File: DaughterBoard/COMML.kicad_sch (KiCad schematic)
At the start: 25 parts, among them J2 PEC03SAAN, J3 PEC02SAAN, J4 PEC02SAAN

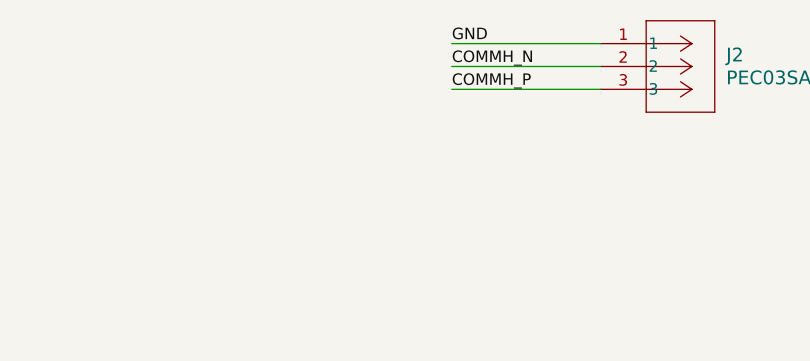
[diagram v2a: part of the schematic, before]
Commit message: DOBO ERC 139 warnings left
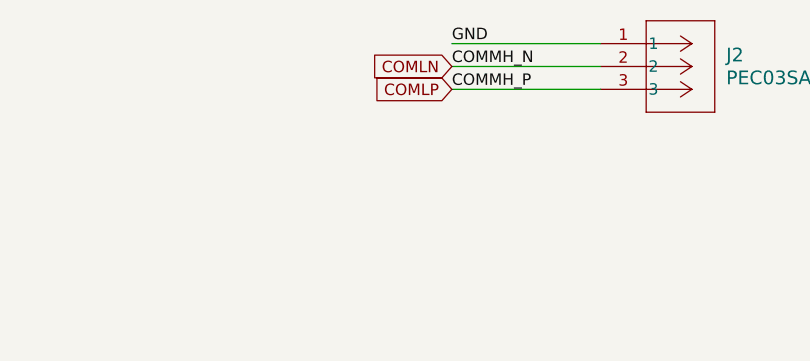
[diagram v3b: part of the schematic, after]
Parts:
- C40, C41: footprint CL10B221JB8NNNC:CAP_CL10_SAM-L -> CAP_CL10_SAM
- C42: footprint GCM1885C1H101JA16J (1):CAPC1608X90N -> GCM1885C1H101JA16J:CAPC1608X90N
- C43, C44: footprint 1206J2K00222KXR (1):CAPC3216X160N -> 1206J2K00222KXR:CAPC3216X160N
- D2: footprint PESD1CAN,215:SOT23_PESD1_NEX-L -> SOT23_PESD1_NEX
- FL1: footprint 744242471:744242471 -> 744242471
- J2: footprint PEC03SAAN:CONN_PEC03SAAN_SUL -> CONN_PEC03SAAN_SUL
- J3, J4: footprint PEC02SAAN:CONN_PxC02S_SUL -> CONN_PxC02S_SUL
- R34, R35: footprint CRCW060351R0JNEA:RC0603N_VIS-L -> RC0603N_VIS
- R36: footprint ERJ-3EKF1001V:RC0603N_PAN-L -> RC0603N_PAN
- R37, R38: footprint RC0603JR-070RL:RC0603N_YAG-L -> RC0603N_YAG
- R39, R40, R41, R42, R43, R44, R45, R46, R47, R48: footprint CRCW08050000Z0EAHP:RES_CRCW_0805_VIS-L -> RES_CRCW_0805_VIS
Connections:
- net COMMH_N is gone; now on net COMLN: J2.2
- net COMMH_P is gone; now on net COMLP: J2.3
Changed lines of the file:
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@@
+		)
+	)
+	(global_label "COMLP"
+		(shape input)
+		(at 232.41 31.75 180)
+		(fields_autoplaced yes)
+		(effects
+			(font
+				(size 1.27 1.27)
+			)
+			(justify right)
+		)
+		(property "Intersheetrefs" "${INTERSHEET_REFS}"
+			(at 223.0748 31.75 0)
+			(effects
+				(font
+					(size 1.27 1.27)
+				)
+				(justify right)
+				(hide yes)
+			)
 		)
 	)
@@
 		)
 	)
-	(symbol
+	(global_label "COMLN"
+		(shape input)
+		(at 232.41 29.21 180)
+		(fields_autoplaced yes)
+		(effects
+			(font
+				(size 1.27 1.27)
+			)
+			(justify right)
+		)
+		(property "Intersheetrefs" "${INTERSHEET_REFS}"
+			(at 223.0143 29.21 0)
+			(effects
+				(font
+					(size 1.27 1.27)
+				)
+				(justify right)
+				(hide yes)
+			)
+		)
+	)
+	(symbol
+		(lib_name "CRCW060351R0JNEA_1")
 		(lib_id "CRCW060351R0JNEA:CRCW060351R0JNEA")
 		(at 137.16 101.6 0)
@@
 			)
 		)
-		(property "Footprint" "CRCW060351R0JNEA:RC0603N_VIS-L"
+		(property "Footprint" "RC0603N_VIS"
 			(at 136.906 96.266 0)
 			(effects
@@
 			)
 		)
-		(property "Footprint" "1206J2K00222KXR (1):CAPC3216X160N"
+		(property "Footprint" "1206J2K00222KXR:CAPC3216X160N"
 			(at 102.87 176.53 0)
 			(effects
@@
 			)
 		)
-		(property "Footprint" "PEC03SAAN:CONN_PEC03SAAN_SUL"
+		(property "Footprint" "CONN_PEC03SAAN_SUL"
+			(at 249.174 36.83 0)
+			(effects
+				(font
+					(size 1.27 1.27)
+					(italic yes)
+				)
+				(hide yes)
+			)
+		)
+		(property "Datasheet" "PEC03SAAN"
+			(at 248.666 22.098 0)
+			(effects
+				(font
+					(size 1.27 1.27)
+					(italic yes)
+				)
+				(hide yes)
+			)
+		)
+		(property "Description" ""
 			(at 248.92 26.67 0)
 			(effects
 				(font
 					(size 1.27 1.27)
-					(italic yes)
-				)
-				(hide yes)
-			)
-		)
-		(property "Datasheet" "PEC03SAAN"
-			(at 248.92 26.67 0)
-			(effects
-				(font
-					(size 1.27 1.27)
-					(italic yes)
-				)
-				(hide yes)
-			)
-		)
-		(property "Description" ""
-			(at 248.92 26.67 0)
-			(effects
-				(font
-					(size 1.27 1.27)
 				)
 				(hide yes)
@@
 	)
 	(symbol
-		(lib_name "CRCW08050000Z0EAHP_2")
+		(lib_name "CRCW08050000Z0EAHP_1")
 		(lib_id "CRCW08050000Z0EAHP:CRCW08050000Z0EAHP")
 		(at 77.47 184.15 0)
@@
 			)
 		)
-		(property "Footprint" "CRCW08050000Z0EAHP:RES_CRCW_0805_VIS-L"
+		(property "Footprint" "RES_CRCW_0805_VIS"
 			(at 77.216 188.976 0)
 			(effects
@@
 	)
 	(symbol
+		(lib_name "CRCW08050000Z0EAHP_1")
 		(lib_id "CRCW08050000Z0EAHP:CRCW08050000Z0EAHP")
 		(at 68.58 31.75 0)
@@
 			)
 		)
-		(property "Footprint" "CRCW08050000Z0EAHP:RES_CRCW_0805_VIS-L"
+		(property "Footprint" "RES_CRCW_0805_VIS"
+			(at 68.072 34.798 0)
+			(effects
+				(font
+					(size 1.27 1.27)
+					(italic yes)
+				)
+				(hide yes)
+			)
+		)
+		(property "Datasheet" "CRCW08050000Z0EAHP"
+			(at 68.58 33.274 0)
+			(effects
+				(font
+					(size 1.27 1.27)
+					(italic yes)
+				)
+				(hide yes)
+			)
+		)
+		(property "Description" ""
 			(at 68.58 31.75 0)
 			(effects
 				(font
 					(size 1.27 1.27)
-					(italic yes)
-				)
-				(hide yes)
-			)
-		)
-		(property "Datasheet" "CRCW08050000Z0EAHP"
-			(at 68.58 31.75 0)
-			(effects
-				(font
-					(size 1.27 1.27)
-					(italic yes)
-				)
-				(hide yes)
-			)
-		)
-		(property "Description" ""
-			(at 68.58 31.75 0)
-			(effects
-				(font
-					(size 1.27 1.27)
 				)
 				(hide yes)
@@
 	)
 	(symbol
-		(lib_name "CRCW08050000Z0EAHP_4")
+		(lib_name "CRCW08050000Z0EAHP_1")
 		(lib_id "CRCW08050000Z0EAHP:CRCW08050000Z0EAHP")
 		(at 115.57 157.48 0)
@@
 			)
 		)
-		(property "Footprint" "CRCW08050000Z0EAHP:RES_CRCW_0805_VIS-L"
+		(property "Footprint" "RES_CRCW_0805_VIS"
 			(at 114.3 163.576 0)
 			(effects
@@
 	)
 	(symbol
+		(lib_name "PEC02SAAN_1")
 		(lib_id "PEC02SAAN:PEC02SAAN")
 		(at 242.57 154.94 0)
@@
 			)
 		)
-		(property "Footprint" "PEC02SAAN:CONN_PxC02S_SUL"
+		(property "Footprint" "CONN_PxC02S_SUL"
+			(at 242.57 162.306 0)
+			(effects
+				(font
+					(size 1.27 1.27)
+					(italic yes)
+				)
+				(hide yes)
+			)
+		)
+		(property "Datasheet" "PEC02SAAN"
+			(at 243.078 152.654 0)
+			(effects
+				(font
+					(size 1.27 1.27)
+					(italic yes)
+				)
+				(hide yes)
+			)
+		)
+		(property "Description" ""
 			(at 242.57 154.94 0)
 			(effects
 				(font
 					(size 1.27 1.27)
-					(italic yes)
-				)
-				(hide yes)
-			)
-		)
-		(property "Datasheet" "PEC02SAAN"
-			(at 242.57 154.94 0)
-			(effects
-				(font
-					(size 1.27 1.27)
-					(italic yes)
-				)
-				(hide yes)
-			)
-		)
-		(property "Description" ""
-			(at 242.57 154.94 0)
-			(effects
-				(font
-					(size 1.27 1.27)
 				)
 				(hide yes)
@@
 	)
 	(symbol
-		(lib_name "CRCW08050000Z0EAHP_5")
 		(lib_id "CRCW08050000Z0EAHP:CRCW08050000Z0EAHP")
 		(at 43.18 161.29 0)
@@
 			)
 		)
-		(property "Footprint" "CRCW08050000Z0EAHP:RES_CRCW_0805_VIS-L"
+		(property "Footprint" "RES_CRCW_0805_VIS"
 			(at 43.18 168.656 0)
 			(effects
@@
 	)
 	(symbol
-		(lib_name "CRCW08050000Z0EAHP_7")
+		(lib_name "CRCW08050000Z0EAHP_1")
 		(lib_id "CRCW08050000Z0EAHP:CRCW08050000Z0EAHP")
 		(at 115.57 176.53 0)
@@
 			)
 		)
-		(property "Footprint" "CRCW08050000Z0EAHP:RES_CRCW_0805_VIS-L"
+		(property "Footprint" "RES_CRCW_0805_VIS"
 			(at 114.808 169.926 0)
 			(effects
@@
 			)
 		)
-		(property "Footprint" "PESD1CAN,215:SOT23_PESD1_NEX-L"
+		(property "Footprint" "SOT23_PESD1_NEX"
 			(at 143.764 106.68 0)
 			(effects
@@
 			)
 		)
-		(property "Footprint" "744242471:744242471"
+		(property "Footprint" "744242471"
 			(at 92.71 260.02 0)
 			(effects
@@
 	)
 	(symbol
-		(lib_name "CRCW08050000Z0EAHP_8")
+		(lib_name "CRCW08050000Z0EAHP_1")
 		(lib_id "CRCW08050000Z0EAHP:CRCW08050000Z0EAHP")
 		(at 43.18 49.53 0)
@@
 			)
 		)
-		(property "Footprint" "CRCW08050000Z0EAHP:RES_CRCW_0805_VIS-L"
+		(property "Footprint" "RES_CRCW_0805_VIS"
 			(at 39.624 40.894 0)
 			(effects
@@
 	)
 	(symbol
-		(lib_name "CRCW08050000Z0EAHP_9")
+		(lib_name "CRCW08050000Z0EAHP_1")
 		(lib_id "CRCW08050000Z0EAHP:CRCW08050000Z0EAHP")
 		(at 43.18 31.75 0)
@@
 			)
 		)
-		(property "Footprint" "CRCW08050000Z0EAHP:RES_CRCW_0805_VIS-L"
+		(property "Footprint" "RES_CRCW_0805_VIS"
 			(at 41.402 46.736 0)
 			(effects
@@
 	)
 	(symbol
-		(lib_name "CRCW08050000Z0EAHP_6")
+		(lib_name "CRCW08050000Z0EAHP_1")
 		(lib_id "CRCW08050000Z0EAHP:CRCW08050000Z0EAHP")
 		(at 77.47 148.59 0)
@@
 			)
 		)
-		(property "Footprint" "CRCW08050000Z0EAHP:RES_CRCW_0805_VIS-L"
+		(property "Footprint" "RES_CRCW_0805_VIS"
 			(at 77.216 151.892 0)
 			(effects
@@
 	)
 	(symbol
-		(lib_name "CRCW060351R0JNEA_1")
 		(lib_id "CRCW060351R0JNEA:CRCW060351R0JNEA")
 		(at 137.16 72.39 0)
@@
 			)
 		)
-		(property "Footprint" "CRCW060351R0JNEA:RC0603N_VIS-L"
+		(property "Footprint" "RC0603N_VIS"
 			(at 133.858 61.976 0)
 			(effects
@@
 			)
 		)
-		(property "Footprint" "CL10B221JB8NNNC:CAP_CL10_SAM-L"
+		(property "Footprint" "CAP_CL10_SAM"
 			(at 172.974 118.618 0)
 			(effects
@@
 			)
 		)
-		(property "Footprint" "RC0603JR-070RL:RC0603N_YAG-L"
+		(property "Footprint" "RC0603N_YAG"
 			(at 106.426 90.424 0)
 			(effects
@@
 	)
 	(symbol
-		(lib_name "CRCW08050000Z0EAHP_3")
+		(lib_name "CRCW08050000Z0EAHP_2")
 		(lib_id "CRCW08050000Z0EAHP:CRCW08050000Z0EAHP")
 		(at 44.45 172.72 0)
@@
 			)
 		)
-		(property "Footprint" "CRCW08050000Z0EAHP:RES_CRCW_0805_VIS-L"
+		(property "Footprint" "RES_CRCW_0805_VIS"
 			(at 45.974 164.592 0)
 			(effects
@@
 			)
 		)
-		(property "Footprint" "RC0603JR-070RL:RC0603N_YAG-L"
+		(property "Footprint" "RC0603N_YAG"
 			(at 109.22 74.93 0)
 			(effects
@@
 			)
 		)
-		(property "Footprint" "PEC02SAAN:CONN_PxC02S_SUL"
-			(at 222.25 152.4 0)
+		(property "Footprint" "CONN_PxC02S_SUL"
+			(at 223.266 148.59 0)
 			(effects
 				(font
@@
 			)
 		)
-		(property "Footprint" "ERJ-3EKF1001V:RC0603N_PAN-L"
+		(property "Footprint" "RC0603N_PAN"
 			(at 186.182 79.248 0)
 			(effects
@@
 			)
 		)
-		(property "Footprint" "GCM1885C1H101JA16J (1):CAPC1608X90N"
+		(property "Footprint" "GCM1885C1H101JA16J:CAPC1608X90N"
 			(at 88.9 41.91 0)
 			(effects
@@
 			)
 		)
-		(property "Footprint" "CRCW08050000Z0EAHP:RES_CRCW_0805_VIS-L"
+		(property "Footprint" "RES_CRCW_0805_VIS"
 			(at 67.056 38.1 0)
 			(effects
@@
 			)
 		)
-		(property "Footprint" "1206J2K00222KXR (1):CAPC3216X160N"
+		(property "Footprint" "1206J2K00222KXR:CAPC3216X160N"
 			(at 102.87 157.48 0)
 			(effects
@@
 			)
 		)
-		(property "Footprint" "CL10B221JB8NNNC:CAP_CL10_SAM-L"
+		(property "Footprint" "CAP_CL10_SAM"
 			(at 172.212 116.84 0)
 			(effects

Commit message: Reviewing
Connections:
- net at D2.2, R35.2, R37.2: no longer D2.1, R34.2, R38.2
- new net: D2.1, R34.2, R38.2
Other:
- moved on the sheet: J3, J4
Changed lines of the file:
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@@
 	(generator "eeschema")
 	(generator_version "8.0")
-	(paper "A4")
+	(paper "A3")
 	(junction
 		(at 193.04 72.39)
@@
 	)
 	(junction
-		(at 130.81 101.6)
-		(diameter 0)
-		(color 0 0 0 0)
-	)
-	(junction
 		(at 88.9 31.75)
 		(diameter 0)
@@
 	(wire
 		(pts
-			(xy 242.57 149.86) (xy 270.51 149.86)
-		)
-		(stroke
-			(width 0)
-			(type default)
-		)
-	)
-	(wire
-		(pts
-			(xy 270.51 161.29) (xy 222.25 161.29)
+			(xy 256.54 148.59) (xy 248.92 148.59)
+		)
+		(stroke
+			(width 0)
+			(type default)
+		)
+	)
+	(wire
+		(pts
+			(xy 184.15 160.02) (xy 248.92 160.02)
 		)
 		(stroke
@@
 	(wire
 		(pts
-			(xy 242.57 154.94) (xy 242.57 149.86)
+			(xy 256.54 154.94) (xy 256.54 148.59)
 		)
 		(stroke
@@
 	(wire
 		(pts
-			(xy 222.25 152.4) (xy 228.6 152.4)
+			(xy 184.15 157.48) (xy 256.54 157.48)
 		)
 		(stroke
@@
 	(wire
 		(pts
-			(xy 228.6 152.4) (xy 228.6 157.48)
-		)
-		(stroke
-			(width 0)
-			(type default)
-		)
-	)
-	(wire
-		(pts
 			(xy 128.27 157.48) (xy 135.89 157.48)
 		)
@@
 	(wire
 		(pts
-			(xy 130.81 106.68) (xy 130.81 101.6)
+			(xy 130.81 72.39) (xy 130.81 106.68)
 		)
 		(stroke
@@
 	(wire
 		(pts
-			(xy 270.51 149.86) (xy 270.51 161.29)
-		)
-		(stroke
-			(width 0)
-			(type default)
-		)
-	)
-	(wire
-		(pts
-			(xy 222.25 161.29) (xy 222.25 154.94)
+			(xy 248.92 148.59) (xy 248.92 160.02)
 		)
 		(stroke
@@
 	(wire
 		(pts
-			(xy 130.81 101.6) (xy 137.16 101.6)
+			(xy 125.73 101.6) (xy 137.16 101.6)
 		)
 		(stroke
@@
 	(wire
 		(pts
-			(xy 228.6 157.48) (xy 242.57 157.48)
-		)
-		(stroke
-			(width 0)
-			(type default)
-		)
-	)
-	(wire
-		(pts
 			(xy 82.55 72.39) (xy 109.22 72.39)
 		)
@@
 	(wire
 		(pts
-			(xy 125.73 101.6) (xy 130.81 101.6)
-		)
-		(stroke
-			(width 0)
-			(type default)
-		)
-	)
-	(wire
-		(pts
 			(xy 128.27 129.54) (xy 166.37 129.54)
 		)
@@
 		(pts
 			(xy 58.42 165.1) (xy 58.42 161.29)
-		)
-		(stroke
-			(width 0)
-			(type default)
-		)
-	)
-	(wire
-		(pts
-			(xy 130.81 72.39) (xy 130.81 101.6)
 		)
 		(stroke
@@
 	)
 	(label "ISO_COMML_N"
-		(at 228.6 152.4 0)
+		(at 203.2 157.48 0)
 		(fields_autoplaced yes)
 		(effects
@@
 	)
 	(label "ISO_COMML_P"
-		(at 222.25 161.29 0)
+		(at 203.2 160.02 0)
 		(fields_autoplaced yes)
 		(effects
@@
 		(lib_name "PEC02SAAN_1")
 		(lib_id "PEC02SAAN:PEC02SAAN")
-		(at 242.57 154.94 0)
+		(at 256.54 154.94 0)
 		(unit 1)
 		(exclude_from_sim no)
@@
 		(fields_autoplaced yes)
 		(property "Reference" "J3"
-			(at 256.54 154.9399 0)
+			(at 270.51 154.9399 0)
 			(effects
 				(font
@@
 		)
 		(property "Value" "PEC02SAAN"
-			(at 256.54 157.4799 0)
+			(at 270.51 157.4799 0)
 			(effects
 				(font
@@
 		)
 		(property "Footprint" "CONN_PxC02S_SUL"
-			(at 242.57 162.306 0)
+			(at 256.54 162.306 0)
 			(effects
 				(font
@@
 		)
 		(property "Datasheet" "PEC02SAAN"
-			(at 243.078 152.654 0)
+			(at 257.048 152.654 0)
 			(effects
 				(font
@@
 		)
 		(property "Description" ""
-			(at 242.57 154.94 0)
+			(at 256.54 154.94 0)
 			(effects
 				(font
@@
 	(symbol
 		(lib_id "PEC02SAAN:PEC02SAAN")
-		(at 222.25 152.4 0)
+		(at 184.15 157.48 0)
 		(mirror y)
 		(unit 1)
@@
 		(dnp no)
 		(property "Reference" "J4"
-			(at 208.28 152.3999 0)
+			(at 170.18 157.4799 0)
 			(effects
 				(font
@@
 		)
 		(property "Value" "PEC02SAAN"
-			(at 208.28 154.9399 0)
+			(at 170.18 160.0199 0)
 			(effects
 				(font
@@
 		)
 		(property "Footprint" "CONN_PxC02S_SUL"
-			(at 223.266 148.59 0)
+			(at 185.166 153.67 0)
 			(effects
 				(font
@@
 		)
 		(property "Datasheet" "PEC02SAAN"
-			(at 222.25 152.4 0)
+			(at 184.15 157.48 0)
 			(effects
 				(font
@@
 		)
 		(property "Description" ""
-			(at 222.25 152.4 0)
-			(effects
-				(font
+			(at 184.15 157.48 0)
+			(effects
+				(font

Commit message: ready for pcb
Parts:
- removed C42: 100pF, GCM1885C1H101JA16J:CAPC1608X90N, symbol GCM1885C1H101JA16J:GCM1885C1H101JA16J
- removed J2: PEC03SAAN, CONN_PEC03SAAN_SUL, symbol PEC03SAAN:PEC03SAAN
- removed J3, J4: PEC02SAAN, CONN_PxC02S_SUL, symbol PEC02SAAN:PEC02SAAN
- removed R39, R40, R41, R42: 0, RES_CRCW_0805_VIS, symbol CRCW08050000Z0EAHP:CRCW08050000Z0EAHP
- added C42, C45: 220pF, CAP_CL10_SAM, symbol CL10B221JB8NNNC:CL10B221JB8NNNC
- added C46, C47: 2200pF, 1206J2K00222KXR:CAPC3216X160N, symbol 1206J2K00222KXR:1206J2K00222KXR
- added D1: 24V, SOT23_PESD1_NEX, symbol PESD1CAN,215:PESD1CAN_215
- added FL2: 470uH, 744242471, symbol 744242471:744242471
- added J2, J3: 705510038, CONN_70551-xxxx_04_MOL, symbol 0705510038:705510038
- added R39, R40: 0, RC0603N_YAG, symbol RC0603JR-070RL:RC0603JR-070RL
- added R41, R42: 51, RC0603N_VIS, symbol CRCW060351R0JNEA:CRCW060351R0JNEA
- added R49: 1.00K, RC0603N_PAN, symbol ERJ-3EKF1001V:ERJ-3EKF1001V
- added R50, R51, R52, R53, R54, R55: 0, RES_CRCW_0805_VIS, symbol CRCW08050000Z0EAHP:CRCW08050000Z0EAHP
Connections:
- net COMLN: now also C42.2, R42.1, R49.1
- net COMLP: now also C45.2, R41.1, R49.2
- net COMML_N_OPT: now also R39.1, R55.1
- net COMML_P_OPT: now also R40.1, R54.1
- net GND: now also C42.1, C45.1, D1.3
- net ISO_COMML_N: now also J2.1, J3.1, R51.2
- net ISO_COMML_P: now also J2.2, J3.2, R50.2
- new net: C47.2, R55.2
- new net: D1.1, R40.2, R41.2
- new net: D1.2, R39.2, R42.2
- new net: C47.1, FL2.3 (N2-), R53.1
- new net: FL2.2 (N2+), R51.1, R53.2
- new net: C46.1, FL2.4 (N1-), R52.1
- new net: FL2.1 (N1+), R50.1, R52.2
- new net: C46.2, R54.2
- no-connect marks 0 -> 4
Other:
- moved on the sheet: C40, C41, C43, C44, D2, FL1, R34, R35, R36, R37, R38, R43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

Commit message: only fuses left
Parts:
- R36: value 1.00K -> 1k
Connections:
- net COMLN: no longer C42.2, R42.1, R49.1
- net COMLP: no longer C45.2, R41.1, R49.2
- net COMML_N_OPT: no longer R39.1, R55.1
- net COMML_P_OPT: no longer R40.1, R54.1
- net ISO_COMML_N: no longer J3.1, R51.2
- net ISO_COMML_P: no longer J3.2, R50.2
- new net COMHN: C42.2, R42.1, R49.1
- new net COMHP: C45.2, R41.1, R49.2
- new net COMMH_N_OPT: R39.1, R55.1
- new net COMMH_P_OPT: R40.1, R54.1
- new net ISO_COMMH_N: J3.1, R51.2
- new net ISO_COMMH_P: J3.2, R50.2
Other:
- moved on the sheet: C46, C47, FL2, R50, R51, R52, R53, R54, R55

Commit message: m
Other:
- moved on the sheet: J2, J3
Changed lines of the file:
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@@
 	)
 	(no_connect
-		(at 154.94 231.14)
+		(at 138.43 227.33)
 	)
 	(no_connect
-		(at 237.49 228.6)
+		(at 270.51 218.44)
 	)
 	(no_connect
-		(at 237.49 231.14)
+		(at 270.51 220.98)
 	)
 	(no_connect
-		(at 154.94 228.6)
+		(at 138.43 224.79)
 	)
 	(wire
@@
 	(wire
 		(pts
-			(xy 140.97 226.06) (xy 154.94 226.06)
+			(xy 124.46 222.25) (xy 138.43 222.25)
 		)
 		(stroke
@@
 	(wire
 		(pts
-			(xy 140.97 223.52) (xy 154.94 223.52)
+			(xy 124.46 219.71) (xy 138.43 219.71)
 		)
 		(stroke
@@
 	(wire
 		(pts
-			(xy 251.46 226.06) (xy 237.49 226.06)
+			(xy 284.48 215.9) (xy 270.51 215.9)
 		)
 		(stroke
@@
 	(wire
 		(pts
-			(xy 251.46 223.52) (xy 237.49 223.52)
+			(xy 284.48 213.36) (xy 270.51 213.36)
 		)
 		(stroke
@@
 	(global_label "ISO_COMMH_N"
 		(shape input)
-		(at 251.46 223.52 0)
+		(at 284.48 213.36 0)
 		(fields_autoplaced yes)
 		(effects
@@
 		)
 		(property "Intersheetrefs" "${INTERSHEET_REFS}"
-			(at 267.6895 223.52 0)
+			(at 300.7095 213.36 0)
 			(effects
 				(font
@@
 	(global_label "ISO_COMML_N"
 		(shape input)
-		(at 140.97 223.52 180)
+		(at 124.46 219.71 180)
 		(fields_autoplaced yes)
 		(effects
@@
 		)
 		(property "Intersheetrefs" "${INTERSHEET_REFS}"
-			(at 125.0429 223.52 0)
+			(at 108.5329 219.71 0)
 			(effects
 				(font
@@
 	(global_label "ISO_COMML_P"
 		(shape input)
-		(at 140.97 226.06 180)
+		(at 124.46 222.25 180)
 		(fields_autoplaced yes)
 		(effects
@@
 		)
 		(property "Intersheetrefs" "${INTERSHEET_REFS}"
-			(at 125.1034 226.06 0)
+			(at 108.5934 222.25 0)
 			(effects
 				(font
@@
 	(global_label "ISO_COMMH_P"
 		(shape input)
-		(at 251.46 226.06 0)
+		(at 284.48 215.9 0)
 		(fields_autoplaced yes)
 		(effects
@@
 		)
 		(property "Intersheetrefs" "${INTERSHEET_REFS}"
-			(at 267.629 226.06 0)
+			(at 300.649 215.9 0)
 			(effects
 				(font
@@
 	(symbol
 		(lib_id "0705510038:705510038")
-		(at 237.49 223.52 0)
+		(at 270.51 213.36 0)
 		(mirror y)
 		(unit 1)
@@
 		(fields_autoplaced yes)
 		(property "Reference" "J3"
-			(at 223.52 226.0599 0)
+			(at 256.54 215.8999 0)
 			(effects
 				(font
@@
 		)
 		(property "Value" "705510038"
-			(at 223.52 228.5999 0)
+			(at 256.54 218.4399 0)
 			(effects
 				(font
@@
 		)
 		(property "Footprint" "CONN_70551-xxxx_04_MOL"
-			(at 237.49 223.52 0)
+			(at 270.51 213.36 0)
 			(effects
 				(font
@@
 		)
 		(property "Datasheet" "705510038"
-			(at 237.49 223.52 0)
+			(at 270.51 213.36 0)
 			(effects
 				(font
@@
 		)
 		(property "Description" ""
-			(at 237.49 223.52 0)
+			(at 270.51 213.36 0)
 			(effects
 				(font
@@
 	(symbol
 		(lib_id "0705510038:705510038")
-		(at 154.94 223.52 0)
+		(at 138.43 219.71 0)
 		(unit 1)
 		(exclude_from_sim no)
@@
 		(fields_autoplaced yes)
 		(property "Reference" "J2"
-			(at 168.91 226.0599 0)
+			(at 152.4 222.2499 0)
 			(effects
 				(font
@@
 		)
 		(property "Value" "705510038"
-			(at 168.91 228.5999 0)
+			(at 152.4 224.7899 0)
 			(effects
 				(font
@@
 		)
 		(property "Footprint" "CONN_70551-xxxx_04_MOL"
-			(at 154.94 223.52 0)
+			(at 138.43 219.71 0)
 			(effects
 				(font
@@
 		)
 		(property "Datasheet" "705510038"
-			(at 154.94 223.52 0)
+			(at 138.43 219.71 0)
 			(effects
 				(font
@@
 		)
 		(property "Description" ""
-			(at 154.94 223.52 0)
-			(effects
-				(font
+			(at 138.43 219.71 0)
+			(effects
+				(font

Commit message: C:/Program Files/Git/
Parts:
- C40, C41, C42, C45: Manufacturer Part Number (none) -> CL10B221JB8NNNC
- C43, C44, C46, C47: Manufacturer Part Number (none) -> 1206J2K00222
- D1, D2: Manufacturer Part Number (none) -> PESD1CAN_215
- FL1, FL2: Manufacturer Part Number (none) -> 744242471
- J2, J3: Manufacturer Part Number (none) -> 0705510038
- R34, R35, R41, R42: Manufacturer Part Number (none) -> CRCW060351R0JNEA
- R36: Manufacturer Part Number (none) -> ERJ-3EKF1001V
- R37, R38, R39, R40: Manufacturer Part Number (none) -> RC0603JR-070RL
- R43, R44, R45, R46, R47, R48, R50, R51, R52, R53, R54, R55: Manufacturer Part Number (none) -> CRCW08050000Z0EAHP
- R49: value 1.00K -> 1K; Manufacturer Part Number (none) -> ERJ-3EKF1001V
